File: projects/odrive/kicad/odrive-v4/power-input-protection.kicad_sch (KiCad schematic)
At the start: 19 parts, among them J1 PC 16/2-ST, Q1 NVMFS5C628NL | BSC027N10NS5

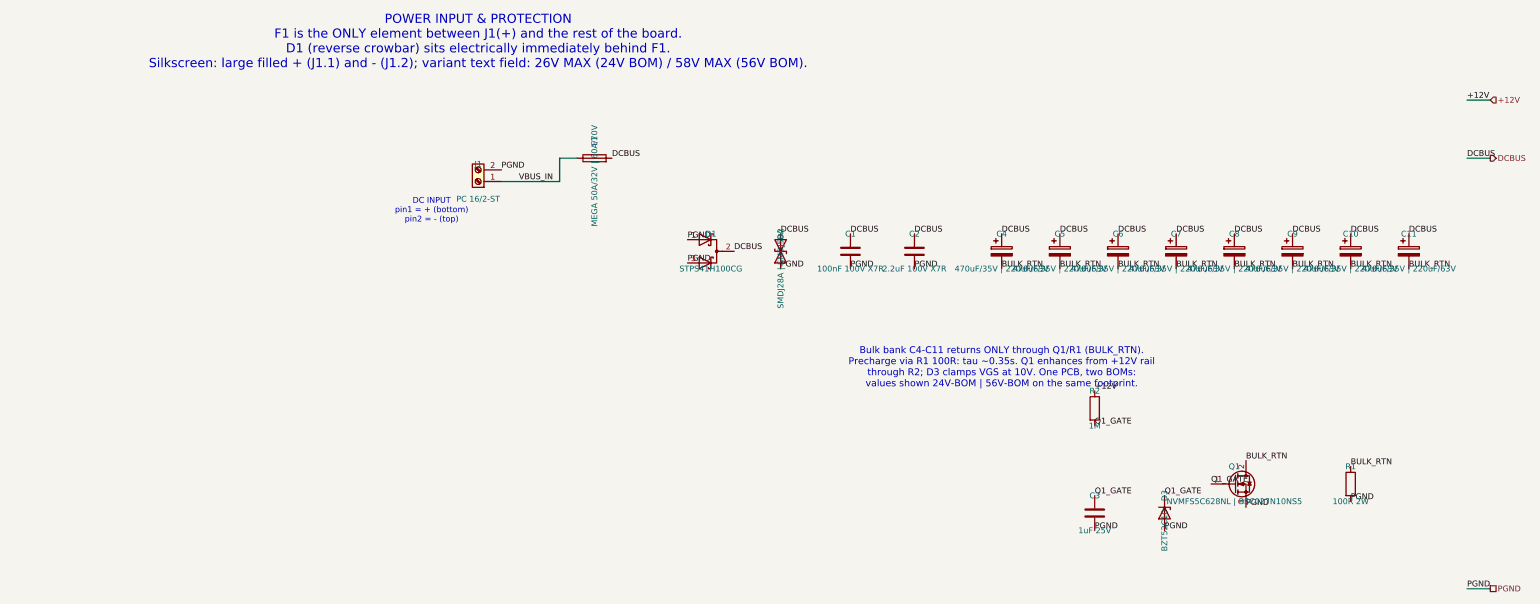
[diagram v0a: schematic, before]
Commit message: Make the v4 schematic sheets readable, netlist-invariant
The verified v4 schematic was electrically perfect and visually unreadable:
connectivity lived in labels stuck on pins, text overlapped, and parts sat
on the title block. Reworked all ten block sheets through Konnect: real
wires for local connections, labels kept for power rails and inter-sheet
nets, parts grouped by function, junction dots where wires join.

The invariant was enforced, not assumed: the exported netlist is diffed
against a reference frozen before the rework - 378 components and 283 nets,
identical membership pin by pin - and ERC holds at 0 errors. The lesson
that forced the rework is now a standing gate: numeric oracles (ERC,
netlist diff, overlap counts) all passed on the unreadable version, so
every sheet is also rendered to PNG and looked at before being declared
done.

An interrupted fix round left one known cosmetic issue, documented in
docs/LOG.md: the encoders-gpio GPIO group's reference/value text fields
float ~134mm right of their symbols, over the title block. konnect 0.2.2
has no tool that repositions property fields, so it waits for 0.11.0.
Also adds the fab footprints the sheets reference (MEGA fuse, Phoenix
terminal blocks, CMC) and restores the board file to the blank template -
the aborted layout skeleton was not worth keeping.
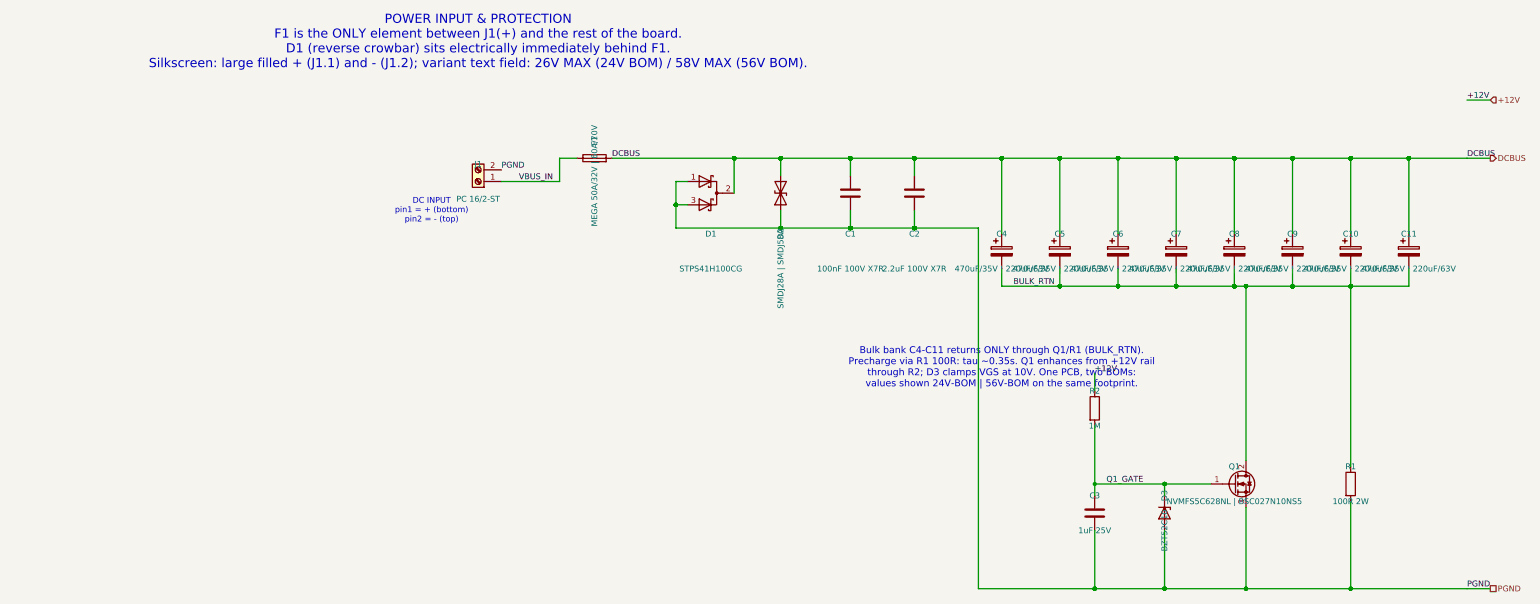
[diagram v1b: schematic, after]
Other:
- moved on the sheet: C1, C2, D1, D2
